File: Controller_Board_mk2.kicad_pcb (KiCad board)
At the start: 2 copper layers, 109.6 x 86.5 mm, 31 parts, among them J1 Barrel_Jack_MountingPin, J2 Barrel_Jack_MountingPin, J3 Barrel_Jack_MountingPin, J4 Barrel_Jack_MountingPin, J5 Barrel_Jack_MountingPin, K1 SANYOU_SRD_Form_C, K2 SANYOU_SRD_Form_C, K3 SANYOU_SRD_Form_C, K4 SANYOU_SRD_Form_C, Q1 BC817, Q2 BC817, Q3 BC817, Q4 BC817, U1 AP63205WU

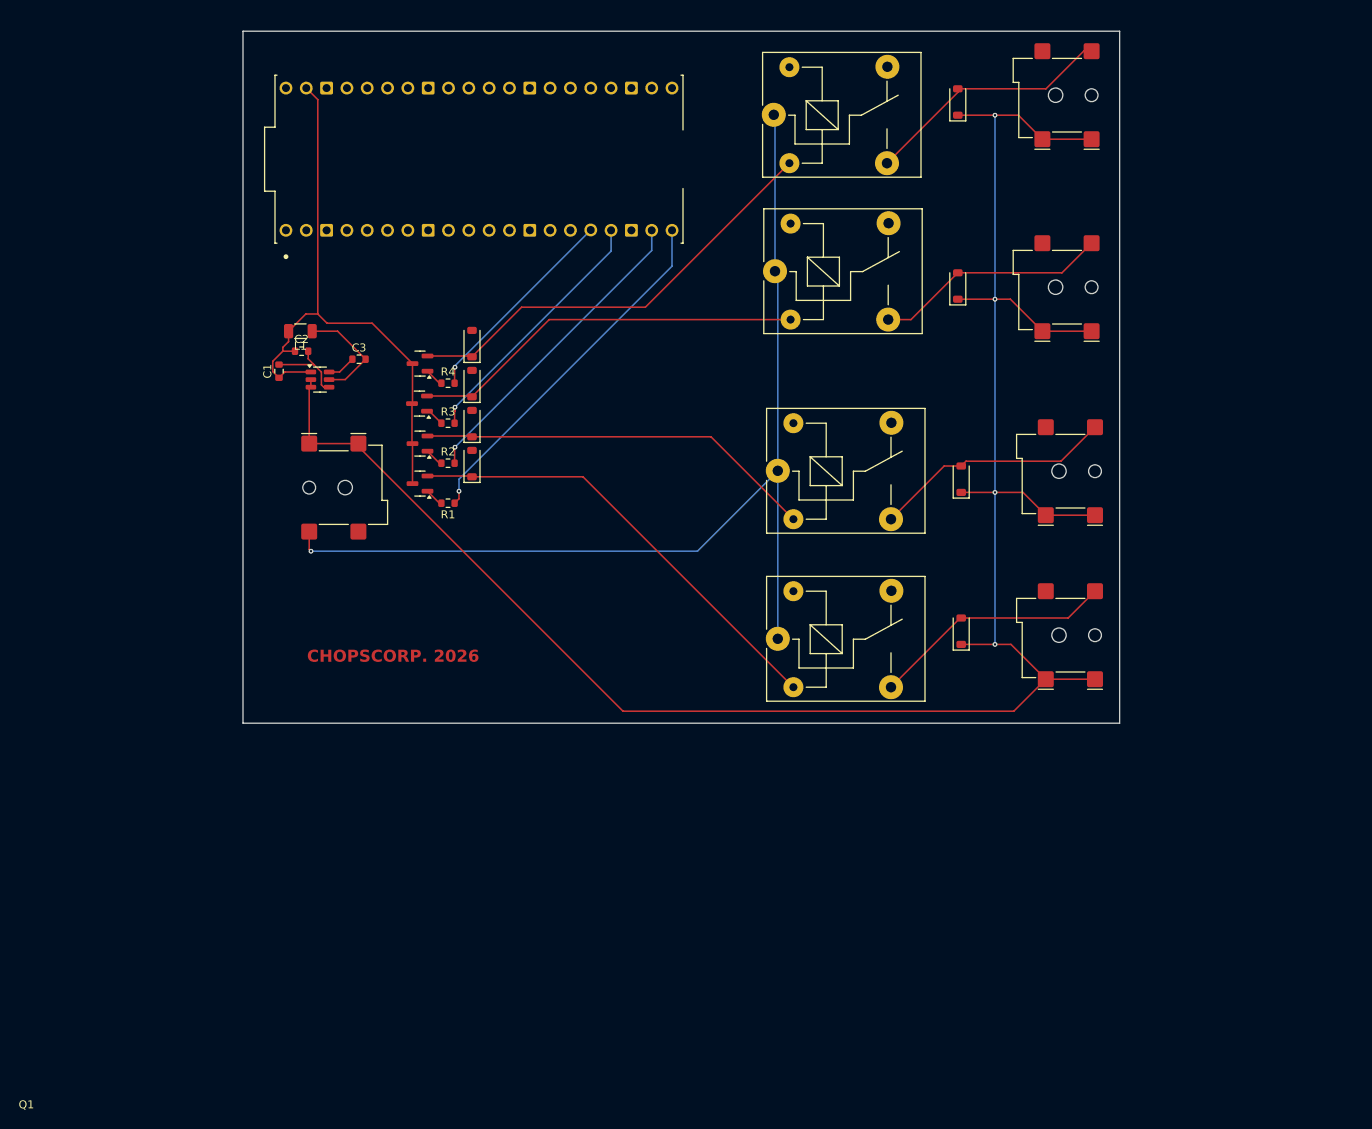
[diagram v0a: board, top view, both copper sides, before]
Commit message: Redid schematic and added fuse sensors
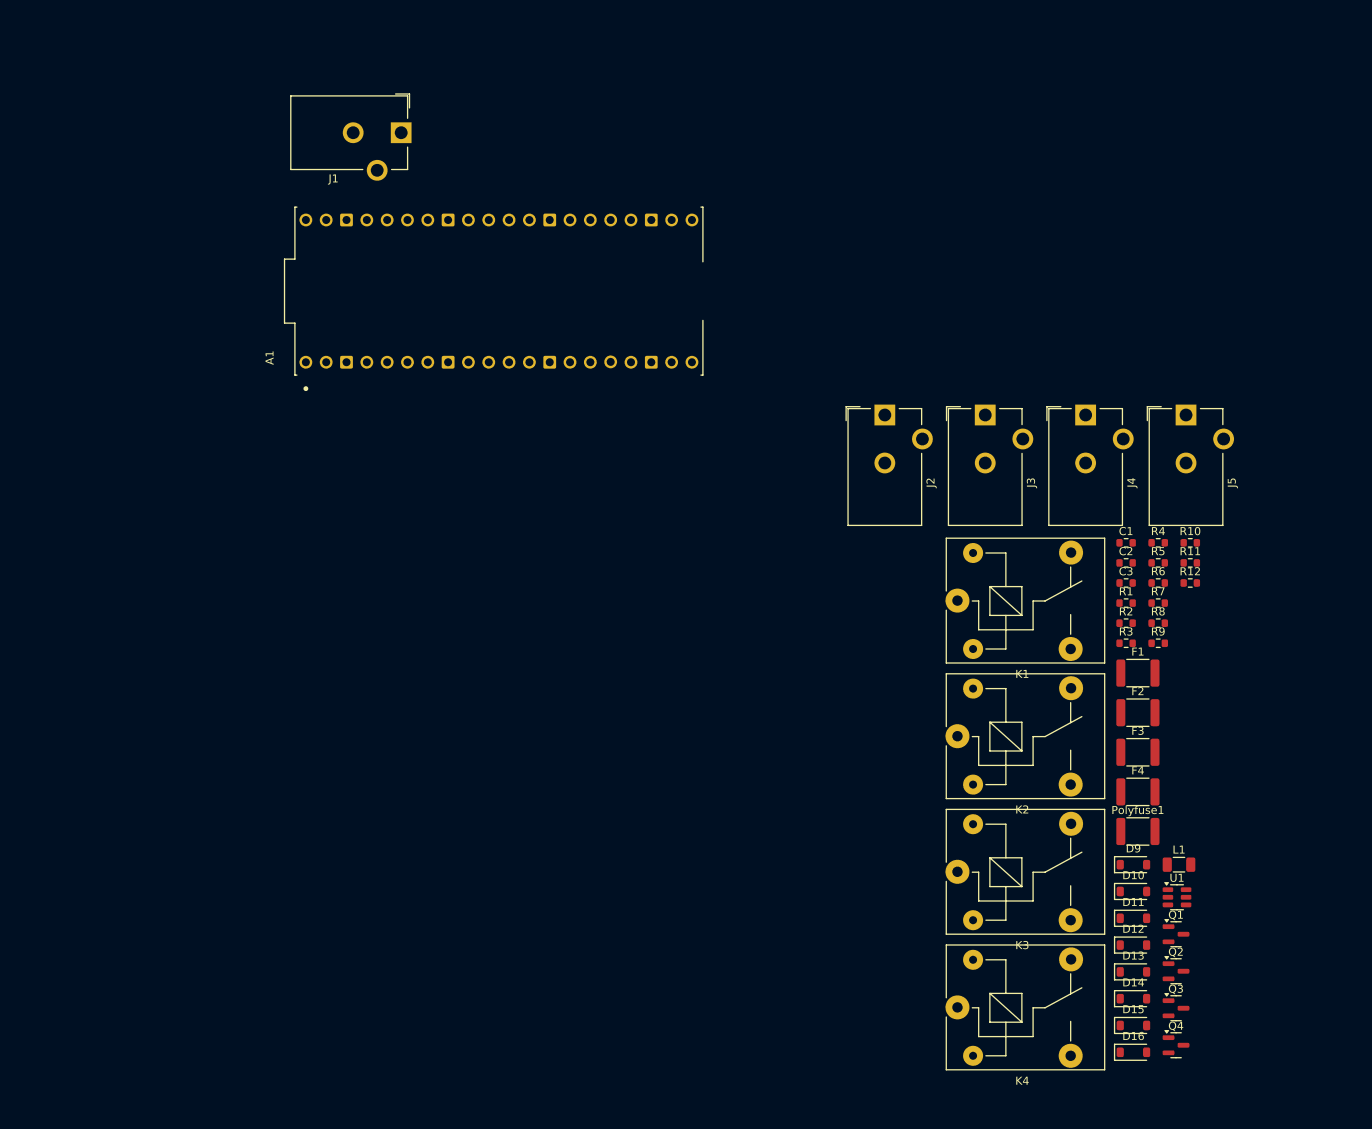
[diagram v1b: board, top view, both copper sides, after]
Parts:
- added F1: RUILONSMD1812P050TF/30, Fuse:Fuse_1812_4532Metric, F.Cu at (126.9, 94.7)
- added F2: RUILONSMD1812P050TF/30, Fuse:Fuse_1812_4532Metric, F.Cu at (126.9, 99.7)
- added F3: RUILONSMD1812P050TF/30, Fuse:Fuse_1812_4532Metric, F.Cu at (126.9, 104.6)
- added F4: RUILONSMD1812P050TF/30, Fuse:Fuse_1812_4532Metric, F.Cu at (126.9, 109.6)
- added Polyfuse1: Littelfuse MINISMDC260F/16-2, Fuse:Fuse_1812_4532Metric, F.Cu at (126.9, 114.5)
- added R10: 33k, Resistor_SMD:R_0603_1608Metric, F.Cu at (133.4, 78.5)
- added R11: 33k, Resistor_SMD:R_0603_1608Metric, F.Cu at (133.4, 81.0)
- added R12: 33k, Resistor_SMD:R_0603_1608Metric, F.Cu at (133.4, 83.5)
- added R5: 100k, Resistor_SMD:R_0603_1608Metric, F.Cu at (129.4, 81.0)
- added R6: 100k, Resistor_SMD:R_0603_1608Metric, F.Cu at (129.4, 83.5)
- added R7: 100k, Resistor_SMD:R_0603_1608Metric, F.Cu at (129.4, 86.0)
- added R8: 100k, Resistor_SMD:R_0603_1608Metric, F.Cu at (129.4, 88.5)
- added R9: 33k, Resistor_SMD:R_0603_1608Metric, F.Cu at (129.4, 91.0)
- J1, J2, J3, J4, J5: footprint Connector_BarrelJack:BarrelJack_Wuerth_694108106102_2.5x5.5mm -> Connector_BarrelJack:BarrelJack_CUI_PJ-102AH_Horizontal
- moved L1 128.5 mm to (132.0, 118.7), turned to 0 degrees
- moved Q4 127.2 mm to (131.6, 141.3), turned to 0 degrees
- moved U1 125.2 mm to (131.8, 122.8)
- moved Q3 121.1 mm to (131.6, 136.6), turned to 0 degrees
- moved D16 120.8 mm to (126.3, 142.1), turned to 0 degrees
- moved Q2 115.2 mm to (131.6, 132.0), turned to 0 degrees
- moved Q1 110.0 mm to (131.6, 127.4), turned to 0 degrees
- moved C1 108.0 mm to (125.4, 78.5), turned to 0 degrees
- moved C2 106.4 mm to (125.4, 81.0)
- moved D9 105.3 mm to (126.3, 118.7), turned to 0 degrees
- moved D10 104.2 mm to (126.3, 122.0), turned to 0 degrees
- moved D11 103.2 mm to (126.3, 125.4), turned to 0 degrees
- moved D12 102.3 mm to (126.3, 128.7), turned to 0 degrees
- moved C3 99.9 mm to (125.4, 83.5)
- moved D15 95.0 mm to (126.3, 138.8), turned to 0 degrees
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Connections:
- A1 pad 1: unconnected-(A1-GP0-Pad1) -> Net-(A1-GP0)
- A1 pad 2: unconnected-(A1-GP1-Pad2) -> Net-(A1-GP1)
- A1 pad 4: unconnected-(A1-GP2-Pad4) -> Net-(A1-GP2)
- A1 pad 5: unconnected-(A1-GP3-Pad5) -> Net-(A1-GP3)
- D15 pad 2: Net-(D15-A) -> Net-(D14-A)
- J1 pad 1: Net-(D13-K) -> Net-(U1-EN)
- J4 pad 2: Net-(D15-A) -> Net-(D14-A)
- K1 pad 3: Net-(D16-A) -> unconnected-(K1-Pad3)
- K1 pad 4: unconnected-(K1-Pad4) -> Net-(D16-A)
- K2 pad 3: Net-(D15-A) -> unconnected-(K2-Pad3)
- K2 pad 4: unconnected-(K2-Pad4) -> Net-(D14-A)
- K3 pad 3: Net-(D14-A) -> unconnected-(K3-Pad3)
- K3 pad 4: unconnected-(K3-Pad4) -> Net-(D14-A)
- K4 pad 3: Net-(D13-A) -> unconnected-(K4-Pad3)
- K4 pad 4: unconnected-(K4-Pad4) -> Net-(D13-A)
- U1 pad 2: Net-(D13-K) -> Net-(U1-EN)
- U1 pad 3: Net-(D13-K) -> Net-(U1-EN)
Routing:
- net Net-(D13-K): track 254.6 -> 0.00 mm, vias 4 -> 0
- net Net-(J1-Pad2): track 130.8 -> 0.00 mm, vias 1 -> 0
- net Net-(A1-VSYS): track 75.9 -> 0.00 mm
- net Net-(D12-K): track 56.7 -> 0.00 mm
- net Net-(D9-K): track 55.3 -> 0.00 mm
- net Net-(D11-K): track 50.0 -> 0.00 mm
- net Net-(D10-K): track 49.5 -> 0.00 mm
- net Net-(A1-GP15): track 45.4 -> 0.00 mm, vias 1 -> 0
- net Net-(A1-GP14): track 39.3 -> 0.00 mm, vias 1 -> 0
- net Net-(A1-GP13): track 32.2 -> 0.00 mm, vias 1 -> 0
- net Net-(D16-A): track 31.6 -> 0.00 mm
- net Net-(D13-A): track 30.5 -> 0.00 mm
- net Net-(D14-A): track 30.3 -> 0.00 mm
- net Net-(D15-A): track 29.4 -> 0.00 mm
- net Net-(A1-GP12): track 26.2 -> 0.00 mm, vias 1 -> 0
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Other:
- board outline removed
- board text removed: "CHOPSCORP. 2026"

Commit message: routed mostly everything and fixed some minor errors
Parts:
- removed D10, D11, D12, D9: 1N4148W, Diode_SMD:D_SOD-123
- added D1: 1N4148W, Diode_SMD:D_SOD-123, F.Cu at (75.2, 17.8)
- added D2: 1N4148W, Diode_SMD:D_SOD-123, F.Cu at (75.2, 23.5)
- added D3: 1N4148W, Diode_SMD:D_SOD-123, F.Cu at (75.2, 29.8)
- added D4: 1N4148W, Diode_SMD:D_SOD-123, F.Cu at (75.2, 35.6)
- moved U1 139.3 mm to (27.9, 29.8)
- moved Q4 133.3 mm to (69.2, 23.5)
- moved L1 131.0 mm to (33.0, 32.8), turned to -90 degrees
- moved Polyfuse1 127.8 mm to (41.3, 19.7)
- moved Q1 126.1 mm to (69.2, 17.8)
- moved Q3 123.5 mm to (69.5, 29.8)
- moved K4 117.9 mm to (81.0, 21.0)
- moved C2 115.1 mm to (21.6, 31.1), turned to 180 degrees
- moved Q2 114.5 mm to (69.8, 35.6)
- moved C1 112.6 mm to (21.6, 34.9), turned to 180 degrees
- moved R9 111.0 mm to (37.5, 28.8), turned to 90 degrees
- moved D13 110.0 mm to (114.7, 22.7), turned to -90 degrees
- moved C3 108.2 mm to (32.2, 28.6)
- moved R5 107.6 mm to (22.9, 65.6), turned to 90 degrees
- moved R10 105.8 mm to (40.0, 28.8), turned to 90 degrees
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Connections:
- A1 pad 10: unconnected-(A1-GP7-Pad10) -> Net-(A1-GP7)
- A1 pad 11: unconnected-(A1-GP8-Pad11) -> Net-(A1-GP8)
- A1 pad 12: unconnected-(A1-GP9-Pad12) -> Net-(A1-GP9)
- A1 pad 16: Net-(A1-GP12) -> unconnected-(A1-GP12-Pad16)
- A1 pad 17: Net-(A1-GP13) -> unconnected-(A1-GP13-Pad17)
- A1 pad 19: Net-(A1-GP14) -> unconnected-(A1-GP14-Pad19)
- A1 pad 20: Net-(A1-GP15) -> unconnected-(A1-GP15-Pad20)
- A1 pad 9: unconnected-(A1-GP6-Pad9) -> Net-(A1-GP6)
- D14 pad 1: Net-(D13-K) -> Net-(D14-K)
- D15 pad 1: Net-(D13-K) -> Net-(D15-K)
- D15 pad 2: Net-(D14-A) -> Net-(D15-A)
- D16 pad 1: Net-(D13-K) -> Net-(D16-K)
- F1 pad 1: Net-(D14-A) -> Net-(D1-K)
- F1 pad 2: Net-(D13-K) -> Net-(D14-K)
- F2 pad 1: Net-(D14-A) -> Net-(D1-K)
- F3 pad 1: Net-(D14-A) -> Net-(D1-K)
- F3 pad 2: Net-(D13-K) -> Net-(D15-K)
- F4 pad 1: Net-(D14-A) -> Net-(D1-K)
- F4 pad 2: Net-(D13-K) -> Net-(D16-K)
- J1 pad 2: Net-(J1-Pad2) -> GND
- J3 pad 1: Net-(D13-K) -> Net-(D14-K)
- J4 pad 1: Net-(D13-K) -> Net-(D15-K)
- J4 pad 2: Net-(D14-A) -> Net-(D15-A)
- J5 pad 1: Net-(D13-K) -> Net-(D16-K)
- K1 pad 1: Net-(J1-Pad2) -> Net-(D16-A)
- K1 pad 2: Net-(D9-K) -> Net-(D1-K)
- K1 pad 4: Net-(D16-A) -> GND
- K1 pad 5: GND -> Net-(D4-A)
- K2 pad 1: Net-(J1-Pad2) -> Net-(D15-A)
- K2 pad 2: Net-(D10-K) -> Net-(D1-K)
- K2 pad 4: Net-(D14-A) -> GND
- K2 pad 5: GND -> Net-(D3-A)
- K3 pad 1: Net-(J1-Pad2) -> Net-(D14-A)
- K3 pad 2: Net-(D11-K) -> Net-(D1-K)
- K3 pad 4: Net-(D14-A) -> GND
- K3 pad 5: GND -> Net-(D2-A)
- K4 pad 1: Net-(J1-Pad2) -> Net-(D13-A)
- K4 pad 2: Net-(D12-K) -> Net-(D1-K)
- K4 pad 4: Net-(D13-A) -> GND
- K4 pad 5: GND -> Net-(D1-A)
- Polyfuse1 pad 2: Net-(D14-A) -> Net-(D1-K)
- Q1 pad 2: Net-(D12-K) -> GND
- Q1 pad 3: Net-(A1-VSYS) -> Net-(D1-A)
- Q2 pad 2: Net-(D11-K) -> GND
- Q2 pad 3: Net-(A1-VSYS) -> Net-(D4-A)
- Q3 pad 2: Net-(D10-K) -> GND
- Q3 pad 3: Net-(A1-VSYS) -> Net-(D3-A)
- Q4 pad 2: Net-(D9-K) -> GND
- Q4 pad 3: Net-(A1-VSYS) -> Net-(D2-A)
- R1 pad 1: Net-(A1-GP15) -> Net-(A1-GP6)
- R2 pad 2: Net-(A1-GP14) -> Net-(A1-GP9)
- R3 pad 2: Net-(A1-GP13) -> Net-(A1-GP8)
- R4 pad 2: Net-(A1-GP12) -> Net-(A1-GP7)
- R6 pad 1: Net-(D13-K) -> Net-(D14-K)
- R7 pad 1: Net-(D13-K) -> Net-(D15-K)
- R8 pad 1: Net-(D13-K) -> Net-(D16-K)
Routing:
- net Net-(D1-K): track 0.00 -> 243.7 mm
- net Net-(D13-K): track 0.00 -> 199.7 mm
- net Net-(D14-K): track 0.00 -> 180.6 mm
- net Net-(D15-K): track 0.00 -> 160.8 mm
- net Net-(D16-K): track 0.00 -> 107.7 mm
- net Net-(A1-GP6): track 0.00 -> 51.3 mm
- net Net-(A1-GP0): track 0.00 -> 44.9 mm
- net Net-(A1-GP7): track 0.00 -> 44.5 mm
- net Net-(A1-GP1): track 0.00 -> 43.9 mm
- net Net-(A1-GP3): track 0.00 -> 42.6 mm
- net Net-(A1-GP2): track 0.00 -> 42.4 mm
- net Net-(A1-GP8): track 0.00 -> 39.1 mm
- net Net-(D4-A): track 0.00 -> 37.2 mm
- net Net-(A1-GP9): track 0.00 -> 34.6 mm
- net Net-(A1-VSYS): track 0.00 -> 32.3 mm
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
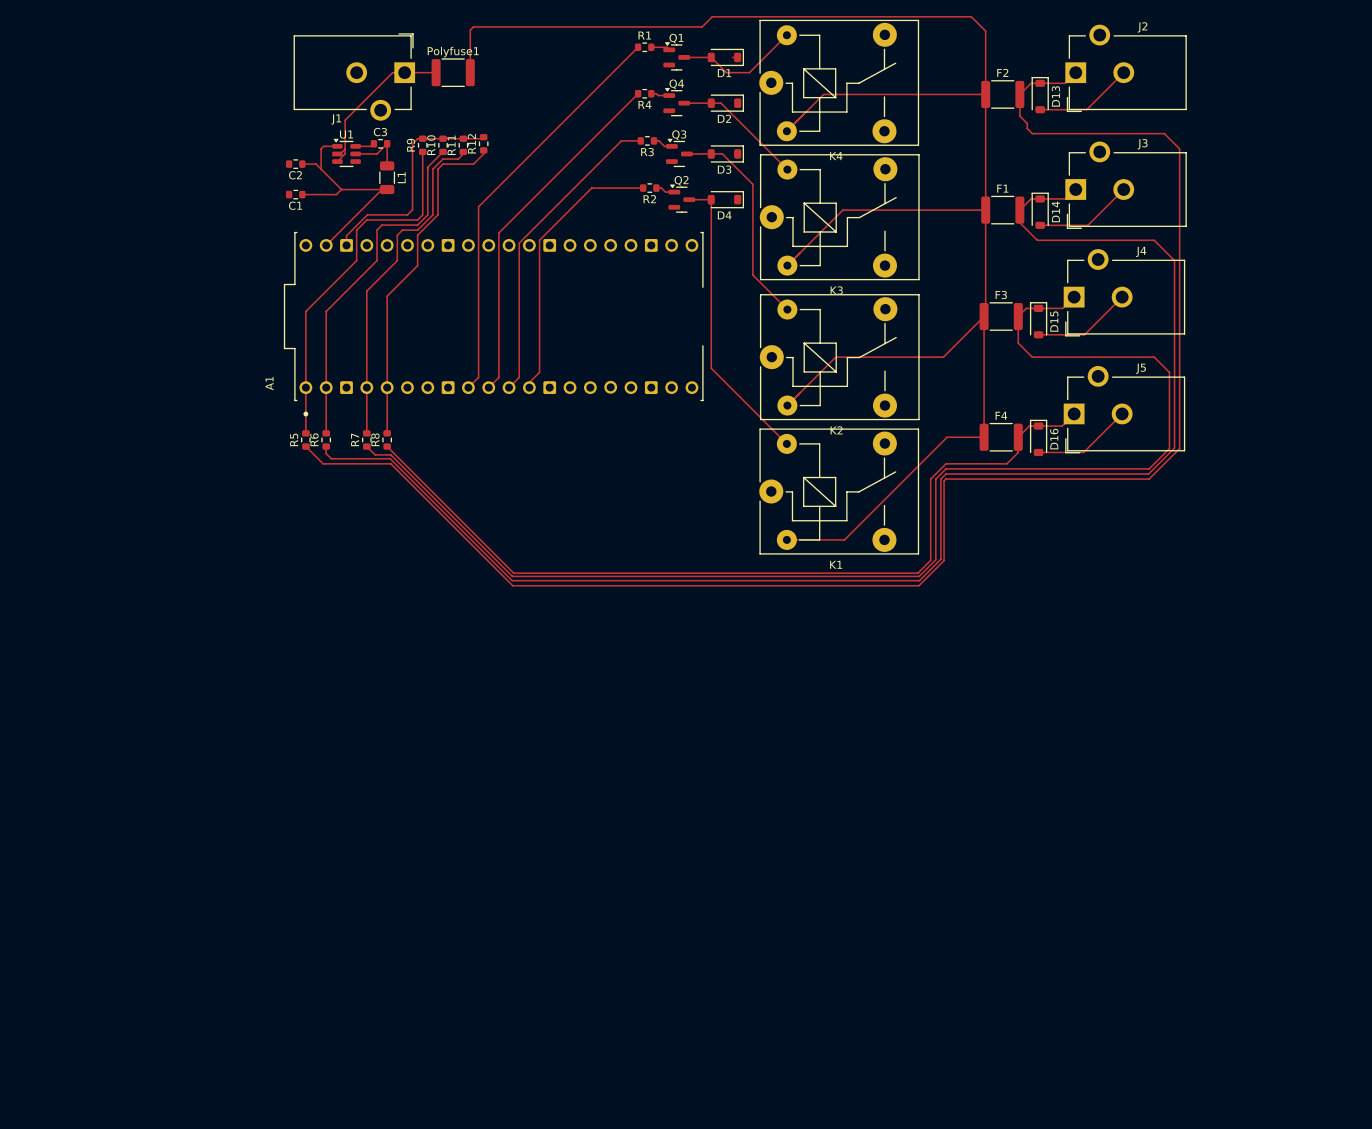
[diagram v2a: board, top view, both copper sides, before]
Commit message: finished routing board, added vias, added gnd plane
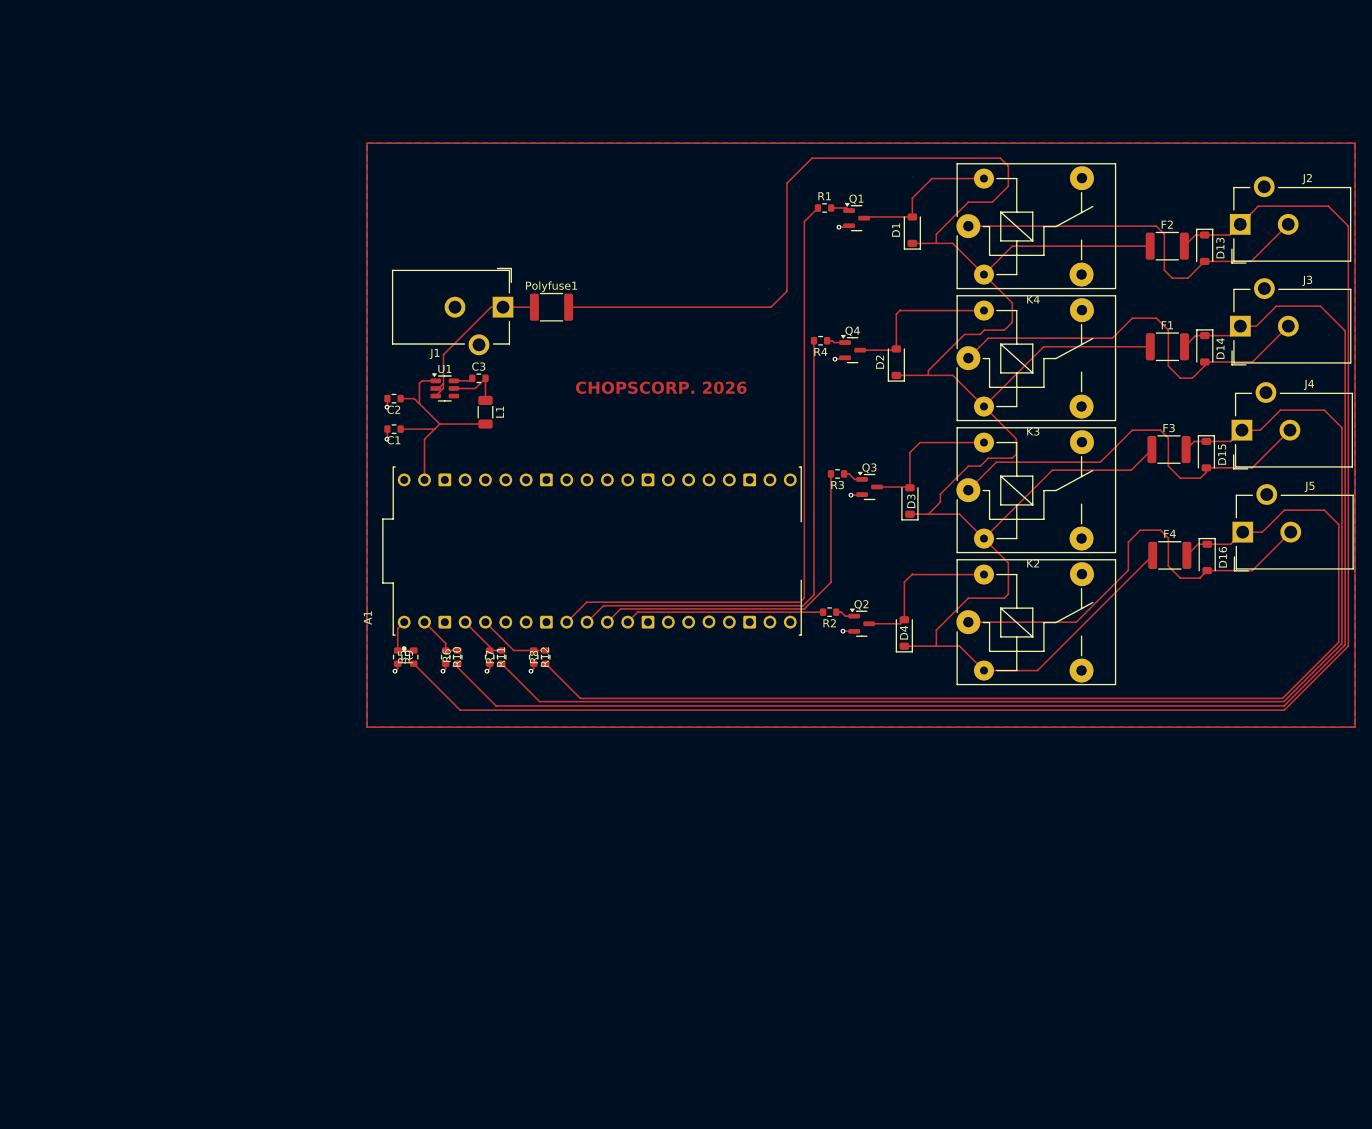
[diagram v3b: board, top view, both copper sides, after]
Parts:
- moved R12 64.5 mm to (51.3, 92.7), turned to -90 degrees
- moved R11 64.1 mm to (45.8, 92.7), turned to -90 degrees
- moved R9 64.1 mm to (34.3, 92.7), turned to -90 degrees
- moved R10 64.0 mm to (40.3, 92.7), turned to -90 degrees
- moved D4 58.6 mm to (97.7, 89.7), turned to 90 degrees
- moved R2 57.6 mm to (88.3, 87.1)
- moved Q2 57.6 mm to (92.3, 88.6)
- moved D3 49.2 mm to (98.4, 73.2), turned to 90 degrees
- moved Q3 47.9 mm to (93.3, 71.5)
- moved R3 47.9 mm to (89.3, 69.8)
- moved D2 38.9 mm to (96.7, 55.9), turned to 90 degrees
- moved Q4 37.9 mm to (91.2, 54.4)
- moved R4 37.9 mm to (87.2, 53.2)
- moved R8 33.6 mm to (52.8, 92.7)
- moved R7 32.0 mm to (47.3, 92.7)
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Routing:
- net Net-(D1-K): track 243.7 -> 295.4 mm
- net Net-(D16-A): track 12.4 -> 54.1 mm
- net Net-(A1-GP0): track 44.9 -> 5.88 mm
- net Net-(D14-A): track 12.3 -> 50.8 mm
- net Net-(D15-A): track 12.4 -> 50.6 mm
- net Net-(A1-GP1): track 43.9 -> 6.64 mm
- net Net-(A1-GP2): track 42.4 -> 6.32 mm
- net Net-(D13-A): track 12.4 -> 48.1 mm
- net Net-(A1-GP3): track 42.6 -> 9.00 mm
- net Net-(D16-K): track 107.7 -> 140.6 mm
- net Net-(A1-GP6): track 51.3 -> 80.4 mm
- net Net-(D4-A): track 37.2 -> 19.7 mm
- net Net-(A1-GP7): track 44.5 -> 61.5 mm
- net GND: track 28.3 -> 12.2 mm, vias 0 -> 10
- net Net-(A1-GP9): track 34.6 -> 25.6 mm
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- added copper zone on B.Cu, net GND
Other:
- board text added: "CHOPSCORP. 2026"

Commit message: added connection from U1 ground to gnd plane
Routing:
- net GND: track 12.2 -> 13.9 mm, vias 10 -> 11
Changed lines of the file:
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@@
+	)
+	(segment
+		(start 41.3675 61.0525)
+		(end 41.91 61.595)
+		(width 0.2)
+		(layer "F.Cu")
+		(net 2)
 	)
 	(segment
@@
 		(start 33.055 65.445)
 		(end 33 65.5)
+		(width 0.2)
+		(layer "F.Cu")
+		(net 2)
+	)
+	(segment
+		(start 41.3675 60.11)
+		(end 41.3675 61.0525)
 		(width 0.2)
 		(layer "F.Cu")
@@
 		(size 0.6)
 		(drill 0.3)
+		(layers "F.Cu" "B.Cu")
+		(free yes)
+		(net 2)
+	)
+	(via
+		(at 41.91 61.595)
+		(size 0.6)
+		(drill 0.3)
